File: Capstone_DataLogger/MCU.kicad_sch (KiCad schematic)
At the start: 13 parts, among them J1 S2B-PH-K-SLFSN, Q1 NMOS, U2 ESP32-DEVKITC-32D, U3 ATmega328-P, U7 SN74HC08N

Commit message: basic changes
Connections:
- net ESP_RX: now also U2.J3-17 (SD1); no longer U2.J3-5 (RXD0)
- net ESP_TX: now also U2.J3-16 (IO15); no longer U2.J3-4 (TXD0)
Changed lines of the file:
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@@
+	)
+	(junction
+		(at 195.58 53.34)
+		(diameter 0)
+		(color 0 0 0 0)
 	)
 	(junction
@@
 	)
 	(no_connect
-		(at 195.58 91.44)
+		(at 195.58 60.96)
 	)
 	(no_connect
@@
 	)
 	(no_connect
-		(at 195.58 93.98)
+		(at 195.58 63.5)
 	)
 	(no_connect
@@
 	(wire
 		(pts
+			(xy 195.58 93.98) (xy 205.74 93.98)
+		)
+		(stroke
+			(width 0)
+			(type default)
+		)
+	)
+	(wire
+		(pts
 			(xy 69.85 66.04) (xy 93.98 66.04)
 		)
@@
 	(wire
 		(pts
+			(xy 195.58 91.44) (xy 205.74 91.44)
+		)
+		(stroke
+			(width 0)
+			(type default)
+		)
+	)
+	(wire
+		(pts
+			(xy 195.58 53.34) (xy 199.39 53.34)
+		)
+		(stroke
+			(width 0)
+			(type default)
+		)
+	)
+	(wire
+		(pts
 			(xy 69.85 50.8) (xy 93.98 50.8)
 		)
@@
 	(wire
 		(pts
+			(xy 194.31 53.34) (xy 195.58 53.34)
+		)
+		(stroke
+			(width 0)
+			(type default)
+		)
+	)
+	(wire
+		(pts
 			(xy 54.61 157.48) (xy 33.02 157.48)
 		)
@@
 	(wire
 		(pts
-			(xy 195.58 60.96) (xy 205.74 60.96)
-		)
-		(stroke
-			(width 0)
-			(type default)
-		)
-	)
-	(wire
-		(pts
 			(xy 90.17 129.54) (xy 90.17 123.19)
 		)
@@
 	(wire
 		(pts
-			(xy 205.74 63.5) (xy 195.58 63.5)
-		)
-		(stroke
-			(width 0)
-			(type default)
-		)
-	)
-	(wire
-		(pts
 			(xy 259.08 74.93) (xy 259.08 76.2)
 		)
@@
 		(pts
 			(xy 59.69 27.94) (xy 54.61 27.94)
-		)
-		(stroke
-			(width 0)
-			(type default)
-		)
-	)
-	(wire
-		(pts
-			(xy 195.58 53.34) (xy 199.39 53.34)
 		)
 		(stroke
@@
 		)
 	)
+	(label "antenna"
+		(at 194.31 53.34 0)
+		(fields_autoplaced yes)
+		(effects
+			(font
+				(size 1.27 1.27)
+			)
+			(justify left bottom)
+		)
+	)
 	(label "5V_CTRL"
 		(at 233.68 36.83 180)
@@
 		)
 	)
+	(label "ESP_TX"
+		(at 198.12 91.44 0)
+		(fields_autoplaced yes)
+		(effects
+			(font
+				(size 1.27 1.27)
+			)
+			(justify left bottom)
+		)
+	)
 	(label "BUZZER"
 		(at 247.65 111.76 0)
@@
 		)
 	)
+	(label "ESP_RX"
+		(at 198.12 93.98 0)
+		(fields_autoplaced yes)
+		(effects
+			(font
+				(size 1.27 1.27)
+			)
+			(justify left bottom)
+		)
+	)
 	(label "ESP_EN"
 		(at 146.05 55.88 0)
@@
 		)
 	)
-	(label "ESP_TX"
-		(at 205.74 60.96 180)
-		(fields_autoplaced yes)
-		(effects
-			(font
-				(size 1.27 1.27)
-			)
-			(justify right bottom)
-		)
-	)
 	(label "BUZZER"
 		(at 71.12 101.6 0)
@@
 		)
 	)
-	(label "ESP_RX"
-		(at 205.74 63.5 180)
-		(fields_autoplaced yes)
-		(effects
-			(font
-				(size 1.27 1.27)
-			)
-			(justify right bottom)
-		)
-	)

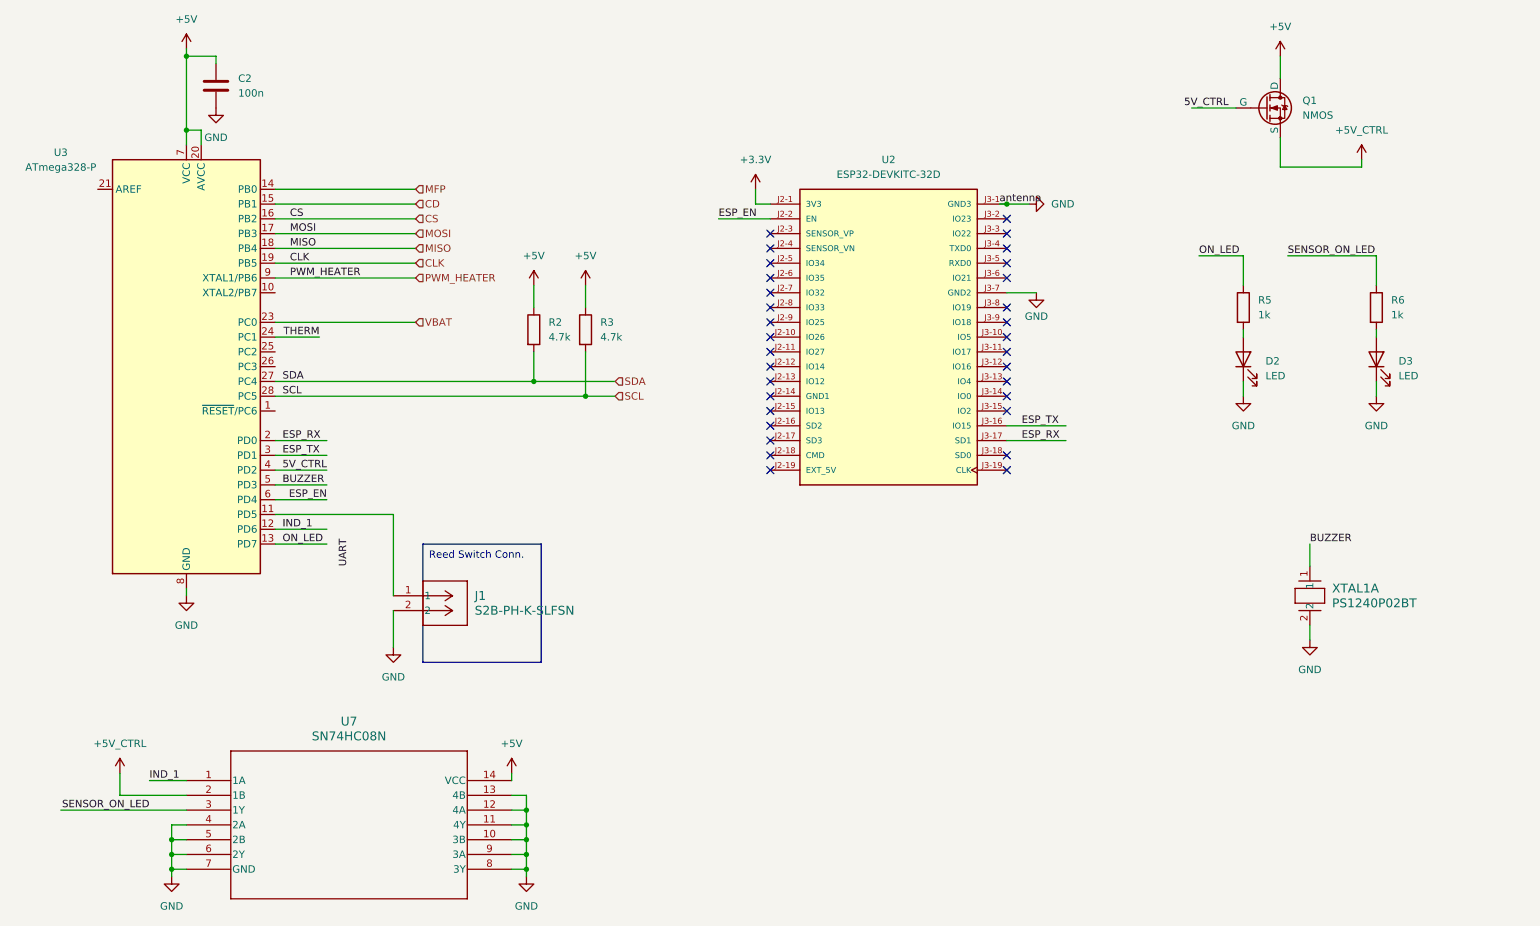
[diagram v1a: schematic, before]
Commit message: pcb connected except SD card
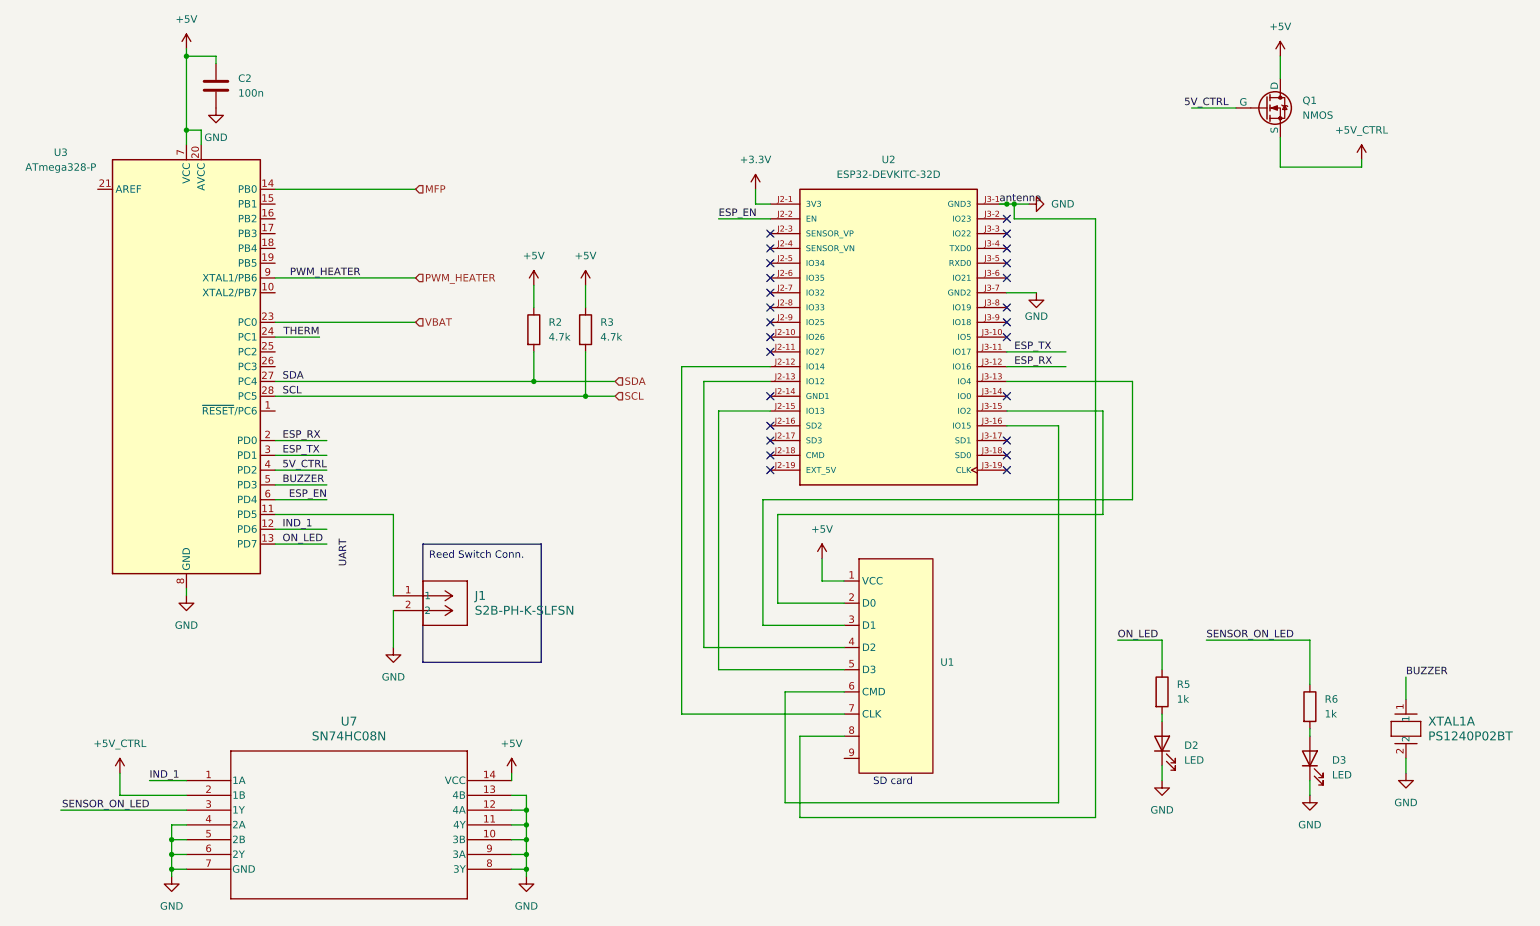
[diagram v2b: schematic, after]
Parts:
- added U1: ~, symbol Capstone:SD_Card
- U2: footprint ESP32-DEVKITC-32D:MODULE_ESP32-DEVKITC-32D -> Capstone:MODULE_ESP32-DEVKITC-32D
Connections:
- net +5V: now also U1.1 (VCC)
- net ESP_RX: now also U2.J3-12 (IO16); no longer U2.J3-17 (SD1)
- net ESP_TX: now also U2.J3-11 (IO17); no longer U2.J3-16 (IO15)
- net GND: now also U1.8
- net at U2.J2-12 (IO14): now also U1.7 (CLK)
- net at U2.J2-13 (IO12): now also U1.4 (D2)
- net at U2.J2-15 (IO13): now also U1.5 (D3)
- net at U2.J3-13 (IO4): now also U1.3 (D1)
- net at U2.J3-15 (IO2): now also U1.2 (D0)
- net CD: no longer names the net of U3.15 (PB1)
- net CLK: no longer names the net of U3.19 (PB5)
- net CS: no longer names the net of U3.16 (PB2)
- net MISO: no longer names the net of U3.18 (PB4)
- net MOSI: no longer names the net of U3.17 (PB3)
- new net: U1.6 (CMD), U2.J3-16 (IO15)
- no-connect marks 32 -> 26
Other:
- note added: "SD card"
- moved on the sheet: D2, D3, R5, R6, XTAL1A

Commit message: pcb connections comeleted
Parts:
- U1: footprint (none) -> Connector_Molex:Molex_Micro-Latch_53253-0970_1x09_P2.00mm_Vertical
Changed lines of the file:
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@@
 		(fields_autoplaced yes)
 		(property "Reference" "U1"
-			(at 184.15 132.0799 0)
+			(at 184.15 130.8099 0)
 			(effects
 				(font
@@
 		)
 		(property "Value" "~"
-			(at 184.15 133.985 0)
+			(at 184.15 132.715 0)
 			(effects
 				(font
@@
 			)
 		)
-		(property "Footprint" ""
-			(at 176.53 120.65 0)
+		(property "Footprint" "Connector_Molex:Molex_Micro-Latch_53253-0970_1x09_P2.00mm_Vertical"
+			(at 184.15 134.6199 0)
 			(effects
 				(font
 					(size 1.27 1.27)
 				)
+				(justify left)
 			)
 		)

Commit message: Revised PCB
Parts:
- removed D2, D3: LED, Diode_SMD:D_1206_3216Metric_Pad1.42x1.75mm_HandSolder, symbol Device:LED
- removed Q1: NMOS, Package_TO_SOT_THT:TO-220-3_Horizontal_TabDown, symbol Simulation_SPICE:NMOS
- removed R5, R6: 1k, Resistor_SMD:R_1206_3216Metric_Pad1.30x1.75mm_HandSolder, symbol Device:R
- removed U7: SN74HC08N, Capstone:N14, symbol Capstone:SN74HC08N
- added J2: S2B-PH-K-SLFSN, Capstone:CONN_S2B-PH-K-S_JST, symbol Capstone:S2B-PH-K-SLFSN
- added R1: 1k, Resistor_SMD:R_1206_3216Metric_Pad1.30x1.75mm_HandSolder, symbol Device:R
- added R4: 10k, symbol Device:R
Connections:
- net +3.3V: now also U1.1 (VCC)
- net +5V: no longer U1.1 (VCC)
- net GND: now also U1.2 (GND), J2.2; no longer J1.2, U1.8
- net THERM: now also U3.23 (PC0); no longer U3.24 (PC1)
- net VBAT: now also U3.25 (PC2); no longer U3.23 (PC0)
- net D0: now reaches U2.J3-15 (IO2)
- net D0: now also U1.3 (D0); no longer U1.2 (D0)
- net D1: now reaches U2.J3-13 (IO4)
- net D1: now also U1.8 (D1); no longer U1.3 (D1)
- net CMD: now reaches U1.4 (CMD)
- net CMD: now also U2.J3-16 (IO15); no longer U2.J2-13 (IO12)
- net CLK: now reaches U1.5 (CLK)
- net CLK: now also U2.J2-12 (IO14); no longer U2.J2-15 (IO13)
- net D3: now reaches U1.6 (D3)
- net D3: now also U2.J2-15 (IO13); no longer U2.J3-16 (IO15)
- net D2: now reaches U1.7 (D2)
- net D2: now also U2.J2-13 (IO12), R4.2; no longer U2.J2-12 (IO14)
- net CD: now reaches U1.9 (CD)
- net at J1.1: now also R1.2; no longer U3.11 (PD5)
- net 5V_CTRL: no longer names the net of U3.4 (PD2)
- net MFP: no longer names the net of U3.14 (PB0)
- new net: J1.2, J2.1
- new net WIFI_STAT: R1.1, U3.24 (PC1)
- no-connect marks 26 -> 27
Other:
- moved on the sheet: J1, XTAL1A

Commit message: Last revision before oreder
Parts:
- added J6: Conn_01x08_Pin, Connector_PinHeader_2.54mm:PinHeader_1x08_P2.54mm_Vertical, symbol Connector:Conn_01x08_Pin
- J1, J2: footprint Capstone:CONN_S2B-PH-K-S_JST -> Capstone:CONN_B2B-XH-A_JST
- R4: footprint (none) -> Resistor_SMD:R_1206_3216Metric_Pad1.30x1.75mm_HandSolder
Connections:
- net +5V: now also J6.2 (Pin_2)
- net GND: now also R4.1, J6.3 (Pin_3)
- net PWM_HEATER: now also U3.15 (PB1); no longer U3.9 (XTAL1/PB6)
- net ~{RESET}: now reaches U3.1 (~{RESET}/PC6)
- net ~{RESET}: now also J6.6 (Pin_6)
- net MOSI: now reaches U3.17 (PB3)
- net MOSI: now also J6.7 (Pin_7)
- net MISO: now reaches U3.18 (PB4)
- net MISO: now also J6.4 (Pin_4)
- net SCK: now reaches U3.19 (PB5)
- net SCK: now also J6.5 (Pin_5)
- net VIBE_SENSE: now reaches U3.26 (PC3)
- net IND_1: no longer names the net of U3.12 (PD6)
- net ON_LED: no longer names the net of U3.13 (PD7)
- no-connect marks 27 -> 33
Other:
- note added: "PICKIT CONN."
- moved on the sheet: R4

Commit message: NVM another revision before order, should be good now
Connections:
- no-connect marks 33 -> 34
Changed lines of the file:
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@@
+	)
+	(no_connect
+		(at 69.85 111.76)
 	)
 	(no_connect

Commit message: Hypothetical final revision of datalogger
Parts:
- added U5: IRLZ34NPBF, Capstone:TO-220AB_INF, symbol Capstone:IRLZ34NPBF
- U1: footprint Connector_Molex:Molex_Micro-Latch_53253-0970_1x09_P2.00mm_Vertical -> Connector_PinHeader_2.54mm:PinHeader_1x09_P2.54mm_Vertical
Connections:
- net ESP_EN: now also U5.1 (GATE); no longer U2.J2-2 (EN)
- net ESP_RX: now also U3.3 (PD1); no longer U3.2 (PD0)
- net ESP_TX: now also U3.2 (PD0); no longer U3.3 (PD1)
- net GND: now also U5.3 (SOURCE)
- net ESP_SLEEP: now reaches U2.J2-11 (IO27)
- net ESP_SLEEP: now also U3.14 (PB0)
- net MFP: now reaches U3.4 (PD2)
- new net: U2.J2-2 (EN), U5.2 (DRAIN)
- no-connect marks 34 -> 35
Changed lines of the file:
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@@
-	)
-	(junction
-		(at 196.85 53.34)
-		(diameter 0)
-		(color 0 0 0 0)
 	)
 	(junction
@@
 	)
 	(no_connect
+		(at 39.37 50.8)
+	)
+	(no_connect
 		(at 69.85 66.04)
 	)
@@
 	)
 	(no_connect
-		(at 154.94 78.74)
-	)
-	(no_connect
 		(at 195.58 63.5)
 	)
@@
 	)
 	(no_connect
+		(at 69.85 55.88)
+	)
+	(no_connect
 		(at 154.94 93.98)
 	)
@@
 	(wire
 		(pts
-			(xy 196.85 53.34) (xy 199.39 53.34)
+			(xy 195.58 53.34) (xy 199.39 53.34)
 		)
 		(stroke
@@
 	(wire
 		(pts
+			(xy 143.51 81.28) (xy 154.94 81.28)
+		)
+		(stroke
+			(width 0)
+			(type default)
+		)
+	)
+	(wire
+		(pts
+			(xy 101.6 53.34) (xy 107.95 53.34)
+		)
+		(stroke
+			(width 0)
+			(type default)
+		)
+	)
+	(wire
+		(pts
 			(xy 59.69 27.94) (xy 59.69 29.21)
 		)
@@
 	(wire
 		(pts
-			(xy 146.05 55.88) (xy 154.94 55.88)
-		)
-		(stroke
-			(width 0)
-			(type default)
-		)
-	)
-	(wire
-		(pts
 			(xy 55.88 153.67) (xy 55.88 154.94)
 		)
@@
 	(wire
 		(pts
-			(xy 144.78 81.28) (xy 154.94 81.28)
-		)
-		(stroke
-			(width 0)
-			(type default)
-		)
-	)
-	(wire
-		(pts
 			(xy 69.85 73.66) (xy 77.47 73.66)
 		)
@@
 	(wire
 		(pts
+			(xy 143.51 78.74) (xy 154.94 78.74)
+		)
+		(stroke
+			(width 0)
+			(type default)
+		)
+	)
+	(wire
+		(pts
 			(xy 54.61 27.94) (xy 54.61 40.64)
 		)
@@
 	(wire
 		(pts
+			(xy 153.67 55.88) (xy 154.94 55.88)
+		)
+		(stroke
+			(width 0)
+			(type default)
+		)
+	)
+	(wire
+		(pts
 			(xy 161.29 137.16) (xy 167.64 137.16)
 		)
@@
 	(wire
 		(pts
-			(xy 195.58 53.34) (xy 196.85 53.34)
-		)
-		(stroke
-			(width 0)
-			(type default)
-		)
-	)
-	(wire
-		(pts
 			(xy 123.19 78.74) (xy 123.19 86.36)
 		)
@@
 	(wire
 		(pts
-			(xy 196.85 55.88) (xy 210.82 55.88)
-		)
-		(stroke
-			(width 0)
-			(type default)
-		)
-	)
-	(wire
-		(pts
 			(xy 148.59 50.8) (xy 148.59 53.34)
 		)
@@
 	(wire
 		(pts
+			(xy 69.85 50.8) (xy 80.01 50.8)
+		)
+		(stroke
+			(width 0)
+			(type default)
+		)
+	)
+	(wire
+		(pts
 			(xy 69.85 93.98) (xy 78.74 93.98)
 		)
@@
 	(wire
 		(pts
+			(xy 69.85 99.06) (xy 78.74 99.06)
+		)
+		(stroke
+			(width 0)
+			(type default)
+		)
+	)
+	(wire
+		(pts
 			(xy 139.7 83.82) (xy 154.94 83.82)
 		)
@@
 	(wire
 		(pts
-			(xy 196.85 53.34) (xy 196.85 55.88)
-		)
-		(stroke
-			(width 0)
-			(type default)
-		)
-	)
-	(wire
-		(pts
 			(xy 69.85 53.34) (xy 80.01 53.34)
 		)
@@
 		(pts
 			(xy 57.15 43.18) (xy 57.15 40.64)
+		)
+		(stroke
+			(width 0)
+			(type default)
+		)
+	)
+	(wire
+		(pts
+			(xy 101.6 55.88) (xy 107.95 55.88)
 		)
 		(stroke
@@
 	(text_box "Ask Steve whether PU or PD"
 		(exclude_from_sim no)
-		(at 132.08 57.15 0)
+		(at 123.19 90.17 0)
 		(size 11.43 7.62)
 		(stroke
@@
 		)
 	)
+	(label "ESP_SLEEP"
+		(at 72.39 50.8 0)
+		(fields_autoplaced yes)
+		(effects
+			(font
+				(size 1.27 1.27)
+			)
+			(justify left bottom)
+		)
+	)
 	(label "D2"
 		(at 161.29 140.97 0)
@@
 		)
 	)
+	(label "ESP_SLEEP"
+		(at 143.51 78.74 0)
+		(fields_autoplaced yes)
+		(effects
+			(font
+				(size 1.27 1.27)
+			)
+			(justify left bottom)
+		)
+	)
 	(label "CD"
 		(at 161.29 148.59 0)
@@
 		)
 	)
+	(label "ESP_EN"
+		(at 101.6 53.34 0)
+		(fields_autoplaced yes)
+		(effects
+			(font
+				(size 1.27 1.27)
+			)
+			(justify left bottom)
+		)
+	)
 	(label "D1"
 		(at 196.85 83.82 0)
@@
 	)
 	(label "ESP_RX"
-		(at 71.12 93.98 0)
-		(fields_autoplaced yes)
-		(effects
-			(font
-				(size 1.27 1.27)
-			)
-			(justify left bottom)
-		)
-	)
-	(label "ESP_RX"
 		(at 196.85 81.28 0)
-		(fields_autoplaced yes)
-		(effects
-			(font
-				(size 1.27 1.27)
-			)
-			(justify left bottom)
-		)
-	)
-	(label "ESP_EN"
-		(at 146.05 55.88 0)
 		(fields_autoplaced yes)
 		(effects
@@
 	)
 	(label "ESP_TX"
-		(at 71.12 96.52 0)
+		(at 72.39 93.98 0)
 		(fields_autoplaced yes)
 		(effects
@@
 	(label "D3"
 		(at 148.59 88.9 0)
+		(fields_autoplaced yes)
+		(effects
+			(font
+				(size 1.27 1.27)
+			)
+			(justify left bottom)
+		)
+	)
+	(label "ESP_RX"
+		(at 72.39 96.52 0)
 		(fields_autoplaced yes)
 		(effects
@@
 		(shape input)
 		(at 77.47 78.74 0)
+		(fields_autoplaced yes)
+		(effects
+			(font
+				(size 1.27 1.27)
+			)
+			(justify left)
+		)
+	)
+	(hierarchical_label "MFP"
+		(shape input)
+		(at 78.74 99.06 0)
 		(fields_autoplaced yes)
 		(effects
@@
 	)
 	(symbol
+		(lib_id "power:GND")
+		(at 101.6 55.88 0)
+		(unit 1)
+		(exclude_from_sim no)
+		(in_bom yes)
+		(on_board yes)
+		(dnp no)
+		(fields_autoplaced yes)
+		(property "Reference" "#PWR021"
+			(at 101.6 62.23 0)
+			(effects
+				(font
+					(size 1.27 1.27)
+				)
+				(hide yes)
+			)
+		)
+		(property "Value" "GND"
+			(at 101.6 60.96 0)
+			(effects
+				(font
+					(size 1.27 1.27)
+				)
+			)
+		)
+		(property "Footprint" ""
+			(at 101.6 55.88 0)
+			(effects
+				(font
+					(size 1.27 1.27)
+				)
+				(hide yes)
+			)
+		)
+		(property "Datasheet" ""
+			(at 101.6 55.88 0)
+			(effects
+				(font
+					(size 1.27 1.27)
+				)
+				(hide yes)
+			)
+		)
+		(property "Description" "Power symbol creates a global label with name \"GND\" , ground"
+			(at 101.6 55.88 0)
+			(effects
+				(font
+					(size 1.27 1.27)
+				)
+				(hide yes)
+			)
+		)
+		(pin "1"
+		)
+		(instances
+			(project ""
+				(path "/3b56a84b-c06c-4c22-a01a-903db63bf091/f949971b-4670-4d3c-889e-c2b74a43479a"
+					(reference "#PWR021")
+					(unit 1)
+				)
+			)
+		)
+	)
+	(symbol
 		(lib_id "Capstone:SD_Card")
 		(at 176.53 120.65 0)
@@
 			)
 		)
-		(property "Footprint" "Connector_Molex:Molex_Micro-Latch_53253-0970_1x09_P2.00mm_Vertical"
+		(property "Footprint" "Connector_PinHeader_2.54mm:PinHeader_1x09_P2.54mm_Vertical"
 			(at 184.15 134.6199 0)
 			(effects
@@
 		(on_board yes)
 		(dnp no)
-		(fields_autoplaced yes)
 		(property "Reference" "#PWR01"
 			(at 148.59 54.61 0)
@@
 					(unit 1)
 				)
+			)
+		)
+	)
+	(symbol
+		(lib_id "Capstone:IRLZ34NPBF")
+		(at 107.95 53.34 0)
+		(unit 1)
+		(exclude_from_sim no)
+		(in_bom yes)
+		(on_board yes)
+		(dnp no)
+		(fields_autoplaced yes)
+		(property "Reference" "U5"
+			(at 130.81 43.18 0)
+			(effects
+				(font
+					(size 1.524 1.524)
+				)
+			)
+		)
+		(property "Value" "IRLZ34NPBF"
+			(at 130.81 45.72 0)
+			(effects
+				(font
+					(size 1.524 1.524)
+				)
+			)
+		)
+		(property "Footprint" "Capstone:TO-220AB_INF"
+			(at 107.95 53.34 0)
+			(effects
+				(font
+					(size 1.27 1.27)
+					(italic yes)
+				)
+				(hide yes)
+			)
+		)
+		(property "Datasheet" "IRLZ34NPBF"
+			(at 107.95 53.34 0)
+			(effects
+				(font
+					(size 1.27 1.27)
+					(italic yes)
+				)
+				(hide yes)
+			)
+		)
+		(property "Description" ""
+			(at 107.95 53.34 0)
+			(effects
+				(font
+					(size 1.27 1.27)
+				)
+				(hide yes)
+			)
+		)
+		(pin "2"
+		)
+		(pin "1"
+		)
+		(pin "3"
+		)
+		(instances
+			(project ""
+				(path "/3b56a84b-c06c-4c22-a01a-903db63bf091/f949971b-4670-4d3c-889e-c2b74a43479a"
+					(reference "U5")
+					(unit 1)
+				)
